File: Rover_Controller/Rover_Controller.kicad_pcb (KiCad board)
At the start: 2 copper layers, 137.6 x 81.5 mm, 32 parts, among them Q1 S8050, SW1 EG1218

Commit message: Traces Removed From PCB
Traces were removed so that re-tracing could be done. With a few new SMD components and enhanced component placement re-tracing the whole board was deemed appropriate.
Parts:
- removed S1, S2, S3, S4: 1825910-6, digikey-footprints:Switch_Tactile_THT_6x6mm
- added 5V_Reg_1: L7805, Package_TO_SOT_THT:TO-220F-3_Horizontal_TabDown, F.Cu at (357.3, 70.6)
- added C1: 1uF, Capacitor_SMD:C_0603_1608Metric_Pad1.05x0.95mm_HandSolder, F.Cu at (282.9, 121.5)
- added C2: 1uF, Capacitor_SMD:C_0603_1608Metric_Pad1.05x0.95mm_HandSolder, F.Cu at (278.5, 121.5)
- added JP1: Jumper_NC_Dual, Connector_PinHeader_2.54mm:PinHeader_1x03_P2.54mm_Vertical, F.Cu at (368.1, 64.5)
- added PWR_SW1: SW_SPST, Button_Switch_SMD:SW_DIP_SPSTx01_Slide_9.78x4.72mm_W8.61mm_P2.54mm, F.Cu at (202.1, 59.5)
- added R1: 4.7K, Resistor_SMD:R_0603_1608Metric_Pad1.05x0.95mm_HandSolder, F.Cu at (261.1, 121.5)
- added R10: 10K, Resistor_SMD:R_0603_1608Metric_Pad1.05x0.95mm_HandSolder, F.Cu at (344.2, 88.3)
- added R11: 10K, Resistor_SMD:R_0603_1608Metric_Pad1.05x0.95mm_HandSolder, F.Cu at (300.3, 121.5)
- added R12: 10K, Resistor_SMD:R_0603_1608Metric_Pad1.05x0.95mm_HandSolder, F.Cu at (295.9, 121.5)
- added R13: 10K, Resistor_SMD:R_0603_1608Metric_Pad1.05x0.95mm_HandSolder, F.Cu at (269.8, 121.5)
- added R14: 10K, Resistor_SMD:R_0603_1608Metric_Pad1.05x0.95mm_HandSolder, F.Cu at (287.2, 121.5)
- added R2: 4.7K, Resistor_SMD:R_0603_1608Metric_Pad1.05x0.95mm_HandSolder, F.Cu at (265.5, 121.5)
- added R3: 4.7K, Resistor_SMD:R_0603_1608Metric_Pad1.05x0.95mm_HandSolder, F.Cu at (274.2, 121.5)
- added R4: 510, Resistor_SMD:R_0603_1608Metric_Pad1.05x0.95mm_HandSolder, F.Cu at (291.6, 121.5)
- added R5: 510, Resistor_SMD:R_0603_1608Metric_Pad1.05x0.95mm_HandSolder, F.Cu at (339.5, 100.1)
- added R6: 510, Resistor_SMD:R_0603_1608Metric_Pad1.05x0.95mm_HandSolder, F.Cu at (355.2, 84.6)
- added R7: 10K, Resistor_SMD:R_0603_1608Metric_Pad1.05x0.95mm_HandSolder, F.Cu at (367.2, 73.6)
- added R8: 10K, Resistor_SMD:R_0603_1608Metric_Pad1.05x0.95mm_HandSolder, F.Cu at (348.5, 88.3)
- added R9: 10K, Resistor_SMD:R_0603_1608Metric_Pad1.05x0.95mm_HandSolder, F.Cu at (355.2, 82.1)
- added RV1: R_POT_TRIM_10K, 3362_Trimmer_Pot:3362P-1-103LF, F.Cu at (335.8, 103.5)
- added SW2: SW_SPST, Button_Switch_SMD:SW_SPST_B3S-1000, F.Cu at (347.5, 82.8)
- added SW3: SW_SPST, Button_Switch_SMD:SW_SPST_B3S-1000, F.Cu at (334.6, 94.7)
- added SW4: SW_SPST, Button_Switch_SMD:SW_SPST_B3S-1000, F.Cu at (345.7, 94.7)
- added TANK_DRIVE1: RED, LED_SMD:LED_0603_1608Metric_Pad1.05x0.95mm_HandSolder, F.Cu at (252.4, 121.6)
- ADC1: footprint Package_DIP:DIP-16_W7.62mm_Socket -> Package_SO:SOIC-16_3.9x9.9mm_P1.27mm
- COM1, PWR1: footprint MRDT_Actives:LED_CREE_XLAMP_XPG -> LED_SMD:LED_0603_1608Metric_Pad1.05x0.95mm_HandSolder
- ESP-12E1: footprint MRDT_Controller_Board:ESP8266_nodeMCU -> Rover_Controller:ESP8266_nodeMCU
- I2C_Bus1: footprint Package_DIP:DIP-16_W7.62mm_Socket -> Package_SO:SOIC-16W_7.5x10.3mm_P1.27mm
- JOY1: renamed from Left_Joystick1; value 2-Axis Joystick -> Left_JOY
- JOY2: renamed from Right_Joystick1; value 2-Axis Joystick -> Right_JOY
- SW1: value EG1218 -> SW_SPST; footprint digikey-footprints:Switch_Slide_11.6x4mm_EG1218 -> Button_Switch_SMD:SW_SPST_B3S-1000
- moved ADC1 213.8 mm to (370.0, 56.4)
- moved PWR1 182.5 mm to (256.8, 121.6)
- moved SW1 169.9 mm to (359.5, 76.6)
- moved COM1 167.2 mm to (248.0, 121.6)
- moved I2C_Bus1 163.3 mm to (335.6, 84.5)
- moved R10 57.2 mm to (251.6, 50.0)
- moved R11 57.2 mm to (236.4, 50.3)
- moved R9 57.2 mm to (236.4, 35.0)
- moved R12 57.2 mm to (251.6, 35.8)
- moved 5V_Reg_1 19.2 mm to (189.7, 73.9), turned to 0 degrees
- moved C1 12.5 mm to (218.2, 57.8)
- moved C2 12.5 mm to (218.1, 53.5)
- renumbered 5V_Regulator1 to 5V_Reg_1, BAT1 to BT1, R4 to RV1
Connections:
- ADC1 pad 5: LFT_SEL -> LeftSel
- ADC1 pad 6: RGHT_SEL -> RightSel
- COM1 pad 1: Net-(COM1-Pad1) -> GND
- COM1 pad 2: GND -> Net-(COM1-Pad2)
- I2C_Bus1 pad 7: /P3 -> P3
- PWR1 pad 1: Net-(PWR1-Pad1) -> GND
- PWR1 pad 2: GND -> Net-(PWR1-Pad2)
- SW1 pad 1: Net-(5V_Regulator1-Pad1) -> SW1
- SW1 pad 2: Net-(BAT1-PadPOS) -> GND
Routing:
- net GND: track 445.8 -> 0.00 mm, vias 2 -> 0
- net 5V: track 421.0 -> 0.00 mm, vias 6 -> 0
- net LFT_SEL: track 106.8 -> 0.00 mm, vias 2 -> 0
- net SafeDrive: track 104.8 -> 0.00 mm, vias 1 -> 0
- net SW2: track 104.4 -> 0.00 mm, vias 2 -> 0
- net SW1: track 100.6 -> 0.00 mm, vias 3 -> 0
- net TankDrive: track 98.8 -> 0.00 mm, vias 1 -> 0
- net D0: track 98.1 -> 0.00 mm, vias 1 -> 0
- net RGHT_SEL: track 94.6 -> 0.00 mm, vias 2 -> 0
- net LeftVert: track 90.9 -> 0.00 mm, vias 2 -> 0
- net SW3: track 89.9 -> 0.00 mm
- net V0: track 86.9 -> 0.00 mm
- net SW4: track 84.7 -> 0.00 mm
- net Net-(16x2_LCD1-Pad11): track 84.1 -> 0.00 mm
- net /k: track 81.9 -> 0.00 mm, vias 1 -> 0
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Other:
- board text removed: "OFF"
- board text removed: "ON"

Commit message: Components Re-Configured on PCB
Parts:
- removed the 5V_Reg_1 at (189.7, 73.9)
- removed the 5V_Reg_1 at (357.3, 70.6)
- removed the C1 at (218.2, 57.8)
- removed the C2 at (278.5, 121.5)
- removed the JP1 at (368.1, 64.5)
- removed the R1 at (175.0, 119.4)
- removed the R10 at (251.6, 50.0)
- removed the R11 at (236.4, 50.3)
- removed the R12 at (251.6, 35.8)
- removed the R2 at (185.1, 95.0)
- removed the R3 at (185.1, 98.6)
- removed the R5 at (339.5, 100.1)
- removed the R6 at (355.2, 84.6)
- removed the R7 at (159.9, 118.9)
- removed the R8 at (159.9, 121.7)
- removed the R9 at (236.4, 35.0)
- removed the RV1 at (335.8, 103.5)
- added 5V_Reg_1: TO-252-3_TabPin2, Package_TO_SOT_SMD:TO-252-3_TabPin2, F.Cu at (190.5, 59.7)
- moved R4 217.6 mm to (83.8, 56.8), turned to 90 degrees
- moved ADC1 213.6 mm to (160.8, 99.8)
- moved R7 203.7 mm to (166.6, 109.5), turned to 90 degrees
- moved R14 200.3 mm to (95.8, 62.6), turned to 270 degrees
- moved PWR1 183.3 mm to (83.8, 60.8), turned to 90 degrees
- moved R8 180.4 mm to (169.4, 109.5), turned to 90 degrees
- moved R13 179.0 mm to (100.8, 62.5), turned to 90 degrees
- moved TANK1 171.8 mm to (91.7, 60.8), turned to 90 degrees
- moved COM1 171.2 mm to (87.9, 60.8), turned to 90 degrees
- moved I2C_Bus1 162.3 mm to (174.0, 100.1)
- moved SW1 159.6 mm to (199.9, 73.2), turned to 270 degrees
- moved R10 152.9 mm to (192.5, 68.8), turned to 90 degrees
- moved R9 148.6 mm to (207.3, 68.8), turned to 90 degrees
- moved SW2 147.6 mm to (199.9, 83.6), turned to 270 degrees
- moved SW3 143.3 mm to (192.3, 78.5), turned to 90 degrees
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- renumbered TANK_DRIVE1 to TANK1
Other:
- board text added: "OFF"
- board text added: "ON"
- board text added: "SAFE"
- board text added: "TANK"
- board text removed: "SafeDrive"
- board text removed: "TankDrive"

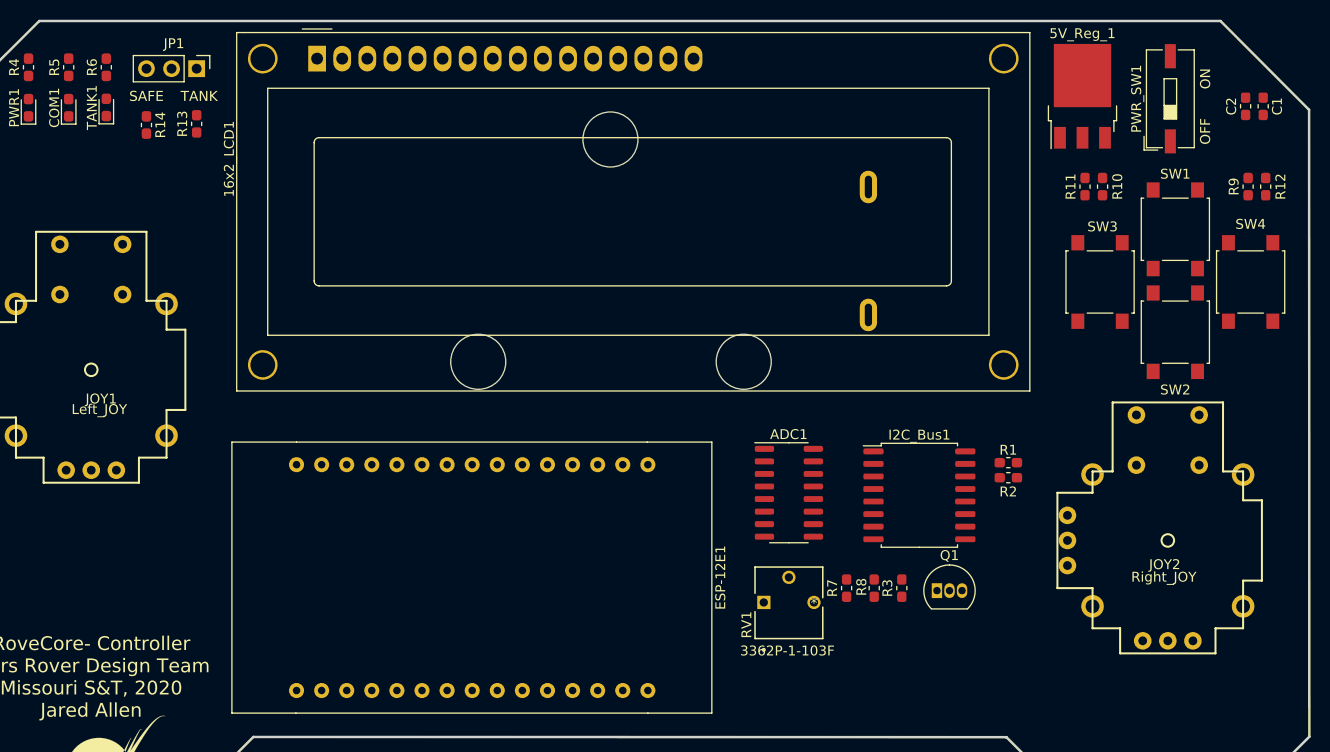
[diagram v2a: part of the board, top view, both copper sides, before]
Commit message: PCB Components Re-Alligned
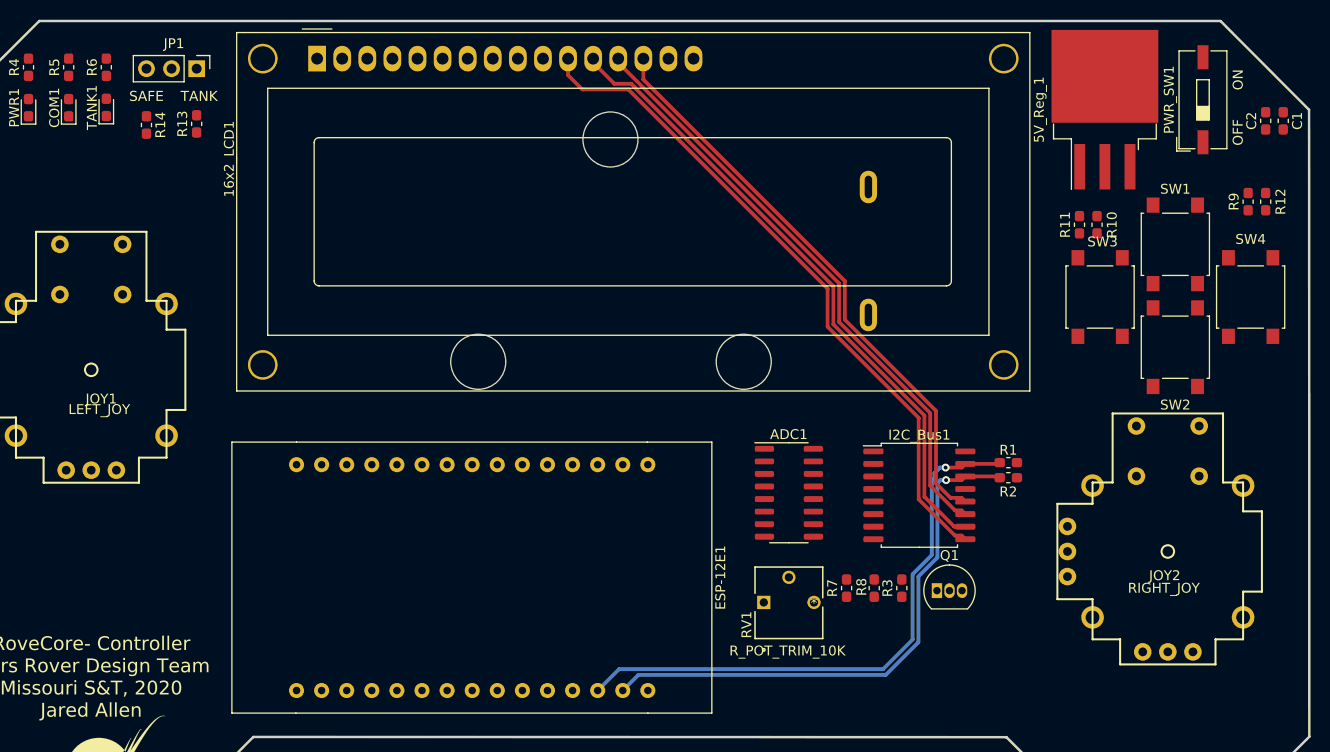
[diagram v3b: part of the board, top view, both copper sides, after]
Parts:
- 5V_Reg_1: value TO-252-3_TabPin2 -> L7805; footprint Package_TO_SOT_SMD:TO-252-3_TabPin2 -> Package_TO_SOT_SMD:TO-263-3_TabPin2
- BT1: value BC9VPC -> 9V_BAT
- JOY1: value Left_JOY -> LEFT_JOY
- JOY2: value Right_JOY -> RIGHT_JOY
- R5, R6: value 100 -> 510
- RV1: value 3362P-1-103F -> R_POT_TRIM_10K; footprint Trimmer_POT_3326:3362P-1-103LF -> 3362_Trimmer_Pot:3362P-1-103LF
- moved R10 3.90 mm to (192.0, 72.7)
- moved R11 3.90 mm to (190.2, 72.7)
- moved PWR_SW1 3.30 mm to (202.7, 60.0)
- moved 5V_Reg_1 2.64 mm to (192.8, 61.0)
- moved C2 2.51 mm to (209.0, 62.2)
- moved C1 2.51 mm to (210.8, 62.2)
- moved R12 1.52 mm to (209.0, 70.4)
- moved R9 1.52 mm to (207.3, 70.4)
- moved SW1 1.52 mm to (199.9, 74.7)
- moved SW2 1.52 mm to (199.9, 85.1)
- moved SW3 1.52 mm to (192.3, 80.0)
- moved SW4 1.52 mm to (207.5, 80.0)
- moved JOY2 1.12 mm to (199.1, 105.8)
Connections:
- net /k renamed k
- 5V_Reg_1 pad 1: (no net) -> Net-(5V_Reg_1-Pad1)
- 5V_Reg_1 pad 2: (no net) -> GND
- 5V_Reg_1 pad 3: (no net) -> 5V
- BT1 pad NEG: GND -> (no net)
- BT1 pad POS: Net-(BAT1-PadPOS) -> (no net)
- C2 pad 1: GND -> 5V
- C2 pad 2: Net-(5V_Regulator1-Pad1) -> GND
- JOY1 pad B1A: LFT_SEL -> LeftSel
- JOY2 pad B1A: RGHT_SEL -> RightSel
- Q1 pad 2: /P3 -> P3
- R5 pad 1: 5V -> D0
- R5 pad 2: Net-(PWR1-Pad1) -> Net-(COM1-Pad2)
- R6 pad 1: D0 -> TankDrive
- R6 pad 2: Net-(COM1-Pad1) -> Net-(R6-Pad2)
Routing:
- net Net-(16x2_LCD1-Pad11): track 0.00 -> 68.5 mm
- net Net-(16x2_LCD1-Pad12): track 0.00 -> 64.6 mm
- net Net-(16x2_LCD1-Pad13): track 0.00 -> 61.0 mm
- net Net-(16x2_LCD1-Pad14): track 0.00 -> 59.0 mm
- net SDA: track 0.00 -> 58.8 mm, vias 0 -> 1
- net SCL: track 0.00 -> 55.5 mm, vias 0 -> 1

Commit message: Traces Updated
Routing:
- net CS: track 0.00 -> 50.1 mm, vias 0 -> 2
- net Din: track 0.00 -> 47.9 mm, vias 0 -> 2
- net Dout: track 0.00 -> 45.8 mm, vias 0 -> 2
- net CLK: track 0.00 -> 43.5 mm, vias 0 -> 2
- net Net-(BT1-Pad1): track 0.00 -> 42.2 mm, vias 0 -> 1
- net Net-(5V_Reg_1-Pad1): track 0.00 -> 32.3 mm
- net SW2: track 0.00 -> 21.9 mm
- net SW1: track 0.00 -> 13.3 mm
- net SW4: track 0.00 -> 13.1 mm
- net SW3: track 0.00 -> 10.5 mm
- net GND: track 0.00 -> 1.75 mm

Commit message: Traces Updated
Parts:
- turned R4 to 270 degrees
- turned R5 to 270 degrees
- turned R6 to 270 degrees
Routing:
- net Net-(16x2_LCD1-Pad4): track 0.00 -> 74.7 mm
- net Net-(16x2_LCD1-Pad5): track 0.00 -> 73.0 mm, vias 0 -> 1
- net Net-(16x2_LCD1-Pad6): track 0.00 -> 71.9 mm, vias 0 -> 1
- net k: track 0.00 -> 65.7 mm, vias 0 -> 1
- net TankDrive: track 0.00 -> 16.2 mm
- net SafeDrive: track 0.00 -> 4.83 mm
- net Net-(PWR1-Pad2): track 0.00 -> 2.34 mm
- net Net-(COM1-Pad2): track 0.00 -> 2.34 mm
- net Net-(R6-Pad2): track 0.00 -> 2.31 mm

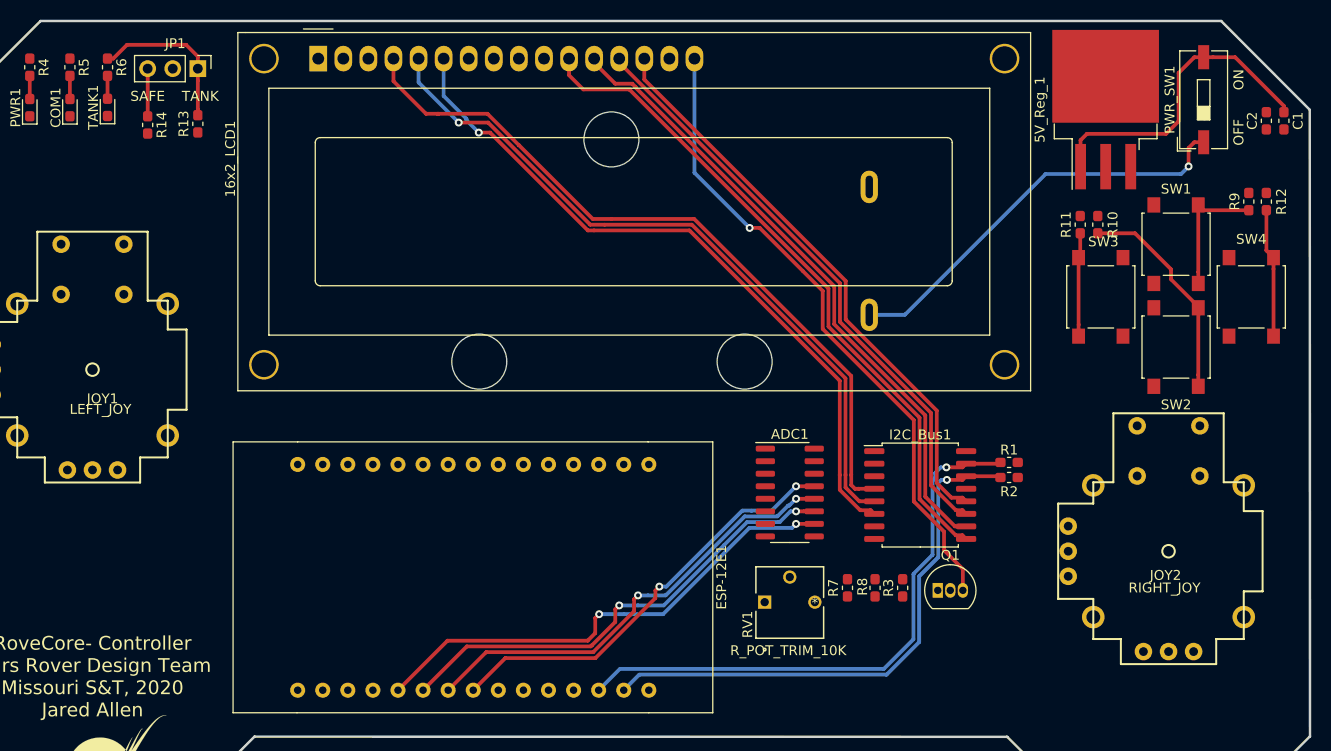
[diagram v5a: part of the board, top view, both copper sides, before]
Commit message: I2C Bus Traces Completed
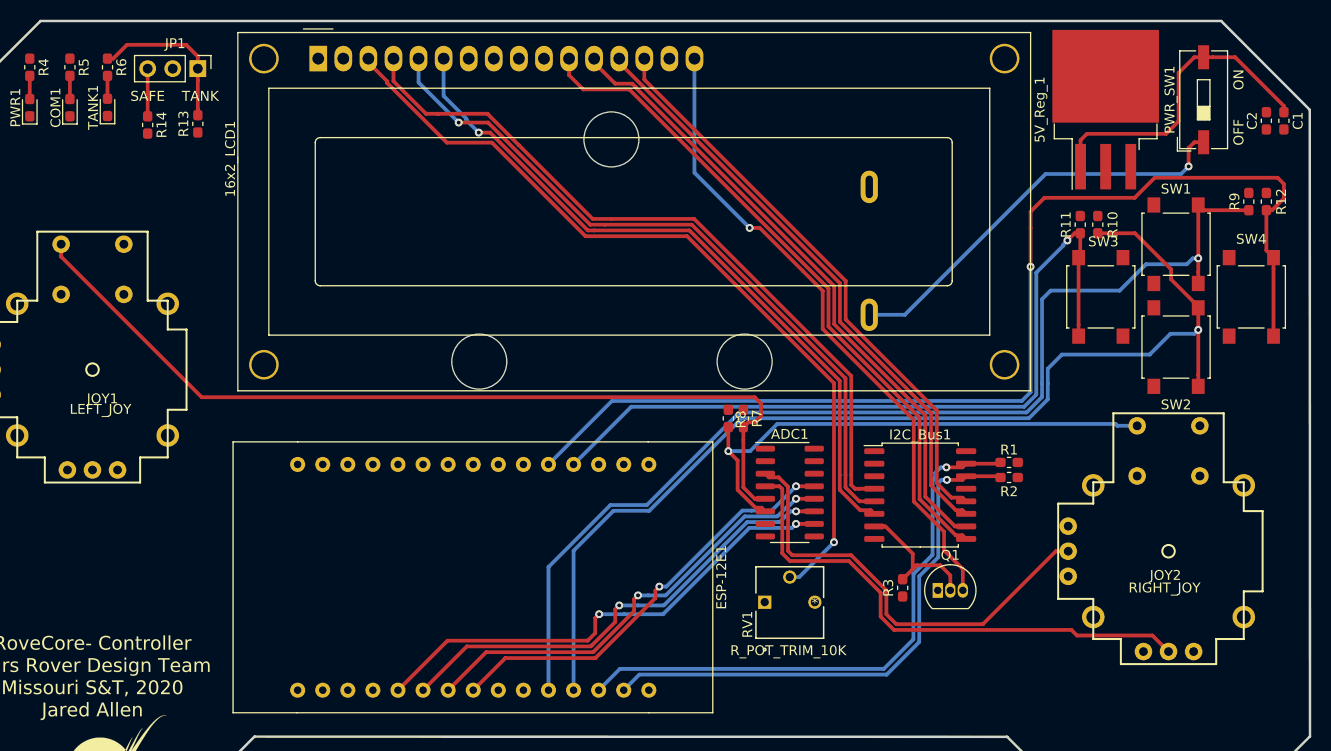
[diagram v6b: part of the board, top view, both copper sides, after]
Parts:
- moved R8 22.7 mm to (154.6, 92.3), turned to 270 degrees
- moved R7 20.1 mm to (156.1, 92.3), turned to 270 degrees
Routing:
- net SW4: track 13.1 -> 114.3 mm, vias 0 -> 1
- net SW1: track 13.3 -> 110.3 mm, vias 0 -> 1
- net LeftSel: track 0.00 -> 90.6 mm
- net SW2: track 21.9 -> 110.4 mm, vias 0 -> 1
- net V0: track 0.00 -> 83.2 mm, vias 0 -> 1
- net SW3: track 10.5 -> 78.8 mm, vias 0 -> 1
- net RightSel: track 0.00 -> 53.1 mm, vias 0 -> 1
- net RightHorz: track 0.00 -> 53.0 mm
- net RightVert: track 0.00 -> 45.3 mm
- net P3: track 0.00 -> 14.0 mm

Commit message: All Traces Placed
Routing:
- net D0: track 0.00 -> 116.5 mm, vias 0 -> 1
- net SafeDrive: track 4.83 -> 90.1 mm, vias 0 -> 2
- net LeftVert: track 0.00 -> 82.6 mm, vias 0 -> 2
- net TankDrive: track 16.2 -> 95.1 mm, vias 0 -> 2
- net LeftHorz: track 0.00 -> 74.9 mm, vias 0 -> 2
- net GND: track 1.75 -> 68.3 mm, vias 0 -> 9
- net 5V: track 0.00 -> 26.8 mm, vias 0 -> 10
- net LeftSel: track 90.6 -> 91.6 mm
- net V0: track 83.2 -> 83.8 mm
- net Net-(5V_Reg_1-Pad1): vias 0 -> 2
- added copper zone on B.Cu, net 5V
- added copper zone on F.Cu, net GND
